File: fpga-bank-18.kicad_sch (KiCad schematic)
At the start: 1 part

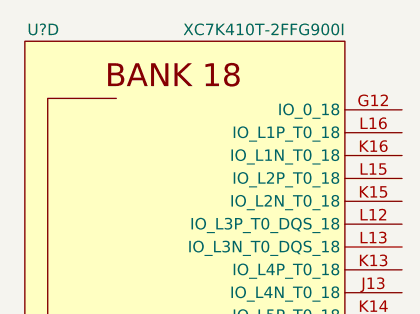
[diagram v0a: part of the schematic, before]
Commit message: Fix FPGA symbol
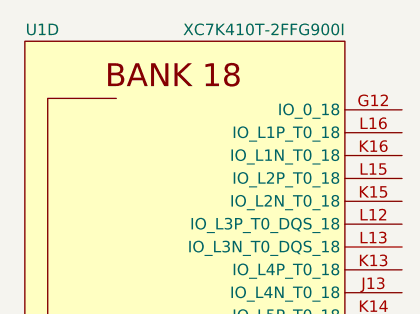
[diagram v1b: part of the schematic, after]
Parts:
- gave numbers to parts that had none: 1
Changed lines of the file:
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@@
     (rev "0.0.99")
   )
-  (symbol (lib_name "XC7K410T-2FFG900I_1") (lib_id "antmicroMicrocontrollers:XC7K410T-2FFG900I") (at 119.38 144.78 0) (unit 4)
+  (symbol (lib_id "antmicroMicrocontrollers:XC7K410T-2FFG900I") (at 119.38 144.78 0) (unit 4)
     (in_bom yes) (on_board yes)
-    (property "Reference" "U?" (id 0) (at 105.41 74.93 0)
+    (property "Reference" "U1" (id 0) (at 105.41 74.93 0)
       (effects (font (size 1.27 1.27)) (justify right))
     )

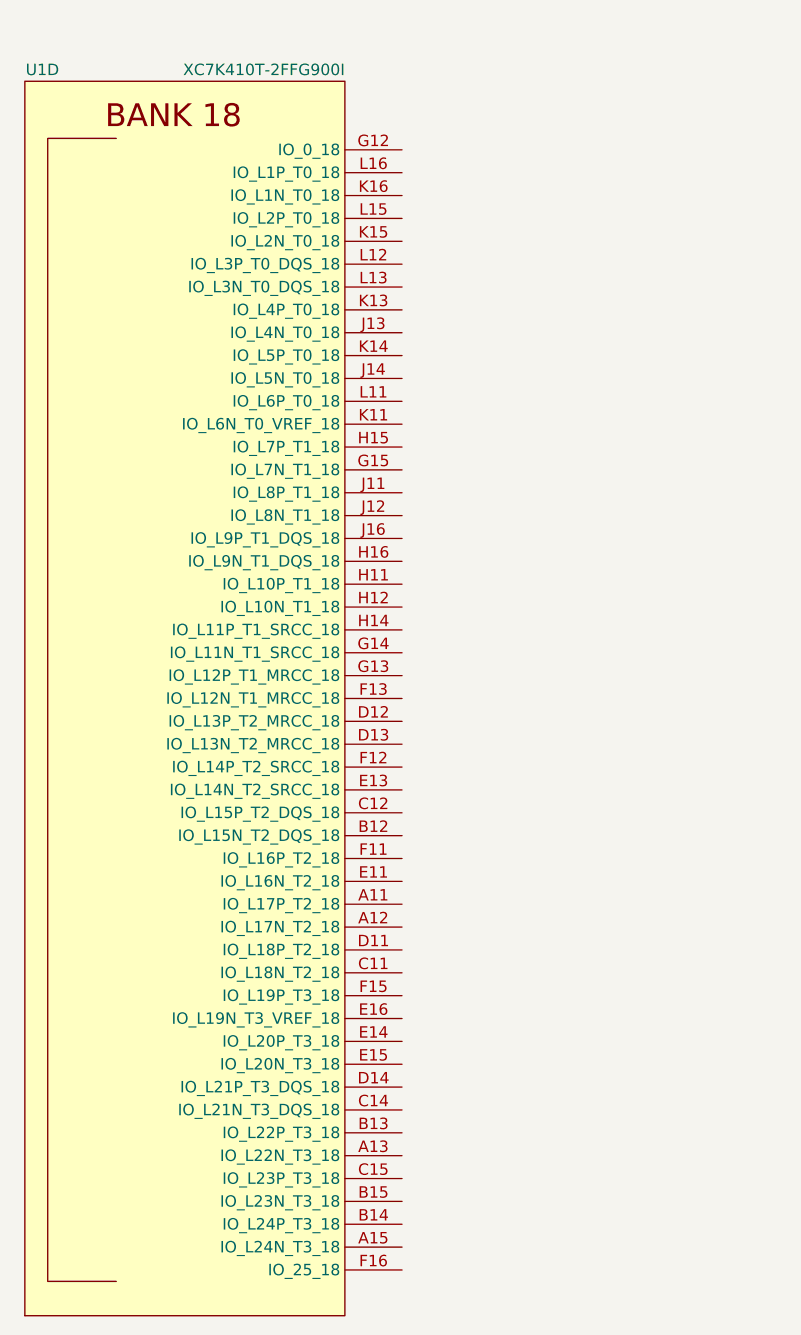
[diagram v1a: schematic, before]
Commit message: Connect IO bank 15 and MGT bank 115 and 116 to FMC+
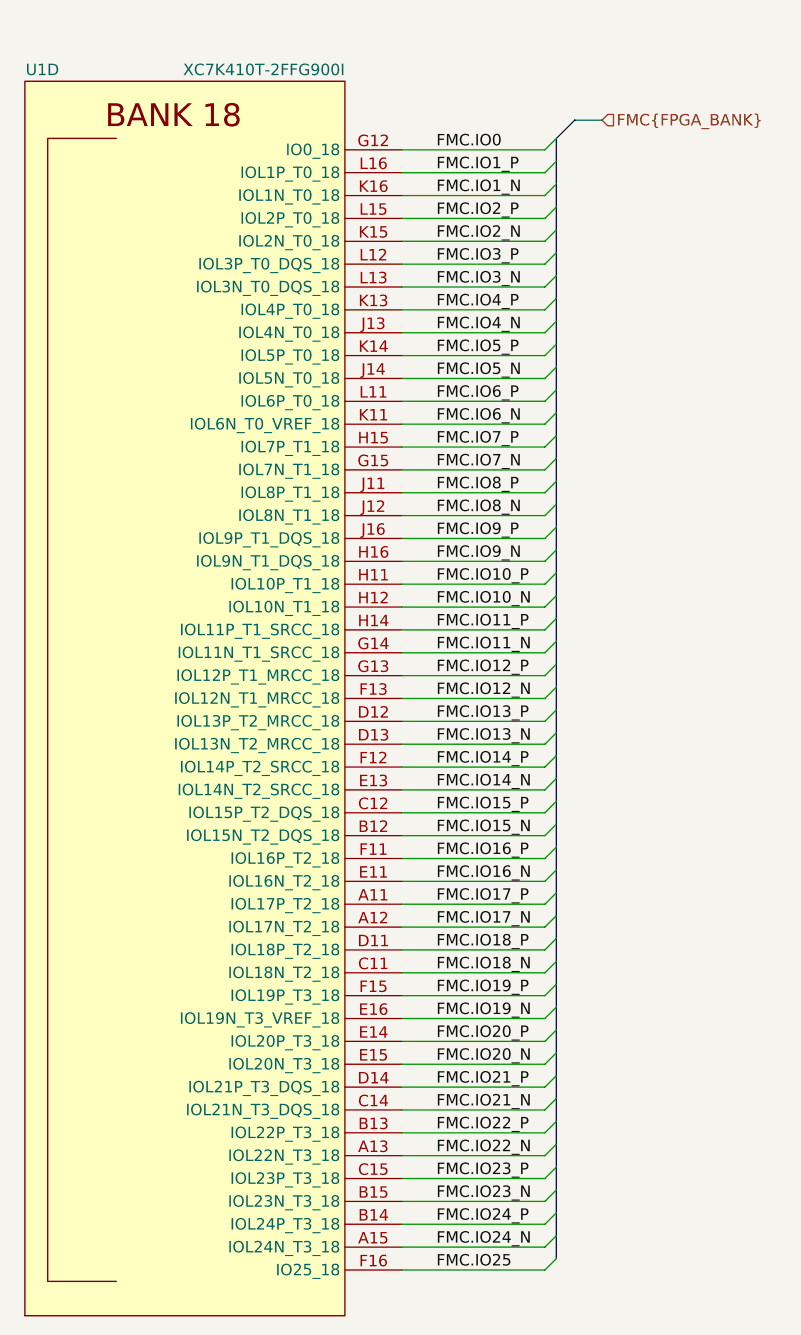
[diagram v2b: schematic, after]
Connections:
- net FMC.IO17_P: now reaches U1.A11 (IOL17P_T2_18)
- net FMC.IO17_N: now reaches U1.A12 (IOL17N_T2_18)
- net FMC.IO22_N: now reaches U1.A13 (IOL22N_T3_18)
- net FMC.IO24_N: now reaches U1.A15 (IOL24N_T3_18)
- net FMC.IO15_N: now reaches U1.B12 (IOL15N_T2_DQS_18)
- net FMC.IO22_P: now reaches U1.B13 (IOL22P_T3_18)
- net FMC.IO24_P: now reaches U1.B14 (IOL24P_T3_18)
- net FMC.IO23_N: now reaches U1.B15 (IOL23N_T3_18)
- net FMC.IO18_N: now reaches U1.C11 (IOL18N_T2_18)
- net FMC.IO15_P: now reaches U1.C12 (IOL15P_T2_DQS_18)
- net FMC.IO21_N: now reaches U1.C14 (IOL21N_T3_DQS_18)
- net FMC.IO23_P: now reaches U1.C15 (IOL23P_T3_18)
- net FMC.IO18_P: now reaches U1.D11 (IOL18P_T2_18)
- net FMC.IO13_P: now reaches U1.D12 (IOL13P_T2_MRCC_18)
- net FMC.IO13_N: now reaches U1.D13 (IOL13N_T2_MRCC_18)
- net FMC.IO21_P: now reaches U1.D14 (IOL21P_T3_DQS_18)
- net FMC.IO16_N: now reaches U1.E11 (IOL16N_T2_18)
- net FMC.IO14_N: now reaches U1.E13 (IOL14N_T2_SRCC_18)
- net FMC.IO20_P: now reaches U1.E14 (IOL20P_T3_18)
- net FMC.IO20_N: now reaches U1.E15 (IOL20N_T3_18)
- net FMC.IO19_N: now reaches U1.E16 (IOL19N_T3_VREF_18)
- net FMC.IO16_P: now reaches U1.F11 (IOL16P_T2_18)
- net FMC.IO14_P: now reaches U1.F12 (IOL14P_T2_SRCC_18)
- net FMC.IO12_N: now reaches U1.F13 (IOL12N_T1_MRCC_18)
- net FMC.IO19_P: now reaches U1.F15 (IOL19P_T3_18)
- net FMC.IO25: now reaches U1.F16 (IO25_18)
- net FMC.IO0: now reaches U1.G12 (IO0_18)
- net FMC.IO12_P: now reaches U1.G13 (IOL12P_T1_MRCC_18)
- net FMC.IO11_N: now reaches U1.G14 (IOL11N_T1_SRCC_18)
- net FMC.IO7_N: now reaches U1.G15 (IOL7N_T1_18)
- net FMC.IO10_P: now reaches U1.H11 (IOL10P_T1_18)
- net FMC.IO10_N: now reaches U1.H12 (IOL10N_T1_18)
- net FMC.IO11_P: now reaches U1.H14 (IOL11P_T1_SRCC_18)
- net FMC.IO7_P: now reaches U1.H15 (IOL7P_T1_18)
- net FMC.IO9_N: now reaches U1.H16 (IOL9N_T1_DQS_18)
- net FMC.IO8_P: now reaches U1.J11 (IOL8P_T1_18)
- net FMC.IO8_N: now reaches U1.J12 (IOL8N_T1_18)
- net FMC.IO4_N: now reaches U1.J13 (IOL4N_T0_18)
- net FMC.IO5_N: now reaches U1.J14 (IOL5N_T0_18)
- net FMC.IO9_P: now reaches U1.J16 (IOL9P_T1_DQS_18)
- net FMC.IO6_N: now reaches U1.K11 (IOL6N_T0_VREF_18)
- net FMC.IO4_P: now reaches U1.K13 (IOL4P_T0_18)
- net FMC.IO5_P: now reaches U1.K14 (IOL5P_T0_18)
- net FMC.IO2_N: now reaches U1.K15 (IOL2N_T0_18)
- net FMC.IO1_N: now reaches U1.K16 (IOL1N_T0_18)
- net FMC.IO6_P: now reaches U1.L11 (IOL6P_T0_18)
- net FMC.IO3_P: now reaches U1.L12 (IOL3P_T0_DQS_18)
- net FMC.IO3_N: now reaches U1.L13 (IOL3N_T0_DQS_18)
- net FMC.IO2_P: now reaches U1.L15 (IOL2P_T0_18)
- net FMC.IO1_P: now reaches U1.L16 (IOL1P_T0_18)

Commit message: Loclib
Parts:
- U1: footprint antmicro-footprints:xc7k410t-2ffg900I -> K410T-devboard-footprints:xc7k410t-2ffg900I; symbol antmicroMicrocontrollers:XC7K410T-2FFG900I -> K410T-devboard:XC7K410T-2FFG900I

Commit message: Bump revision to 1.0.0. Update name on schematic and PCB sheets
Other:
- title: K410T devboard -> Kintex 410T devboard

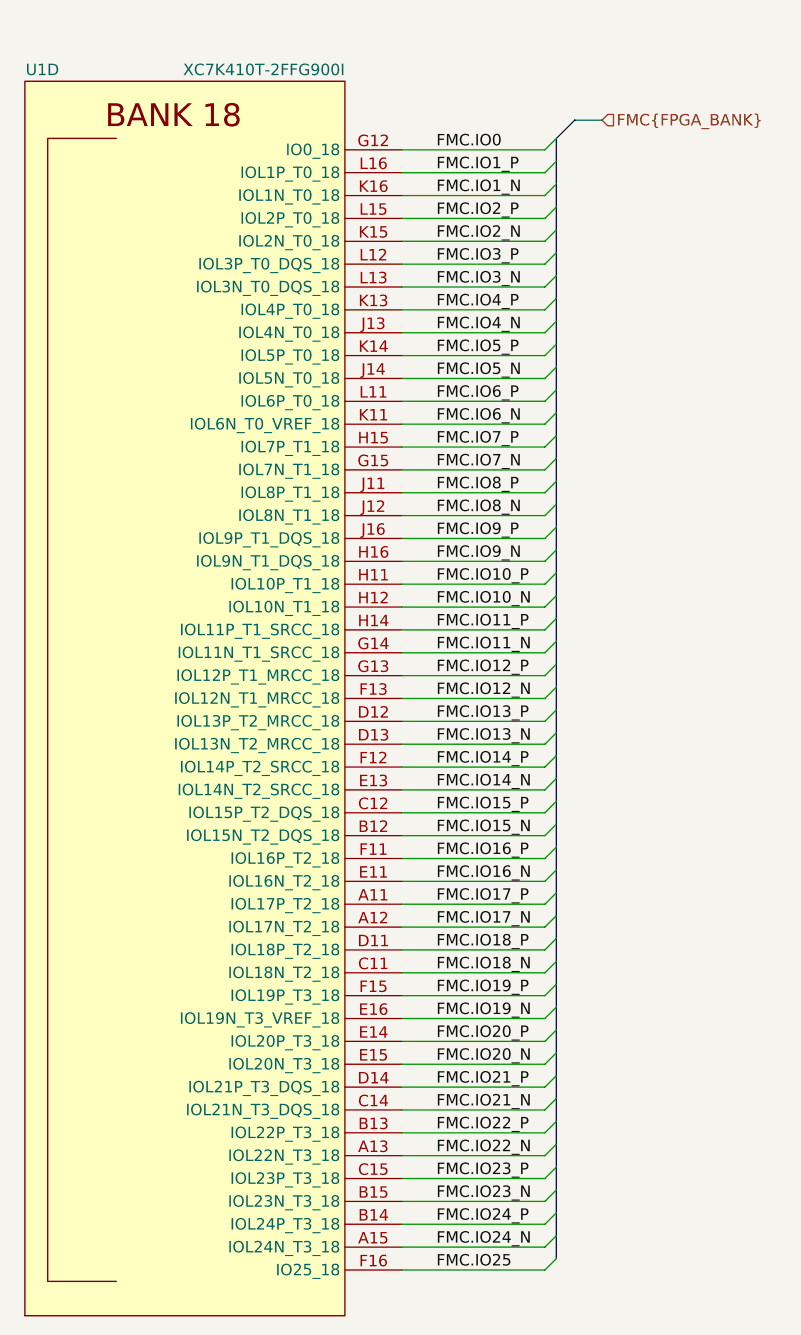
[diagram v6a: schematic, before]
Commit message: Introduce component standardization
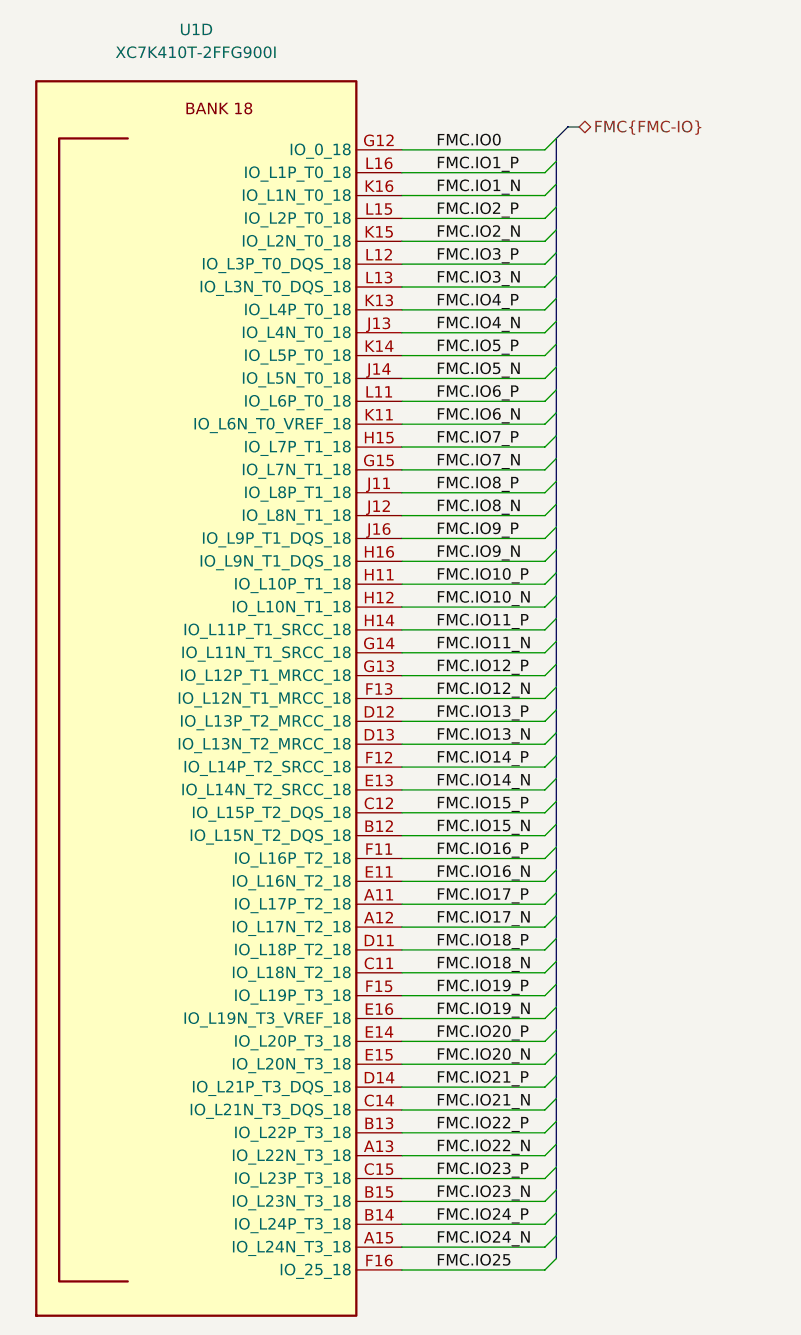
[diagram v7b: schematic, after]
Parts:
- U1: Author (none) -> Antmicro; License (none) -> Apache-2.0
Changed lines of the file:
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@@
     (title "Kintex 410T devboard")
     (date "2023-02-01")
-    (rev "1.0.0")
+    (rev "1.1.1")
   )
   (bus_entry (at 159.385 187.96) (size 1.27 -1.27)
@@
     (stroke (width 0) (type default) (color 0 0 0 0))
   )
+  (bus (pts (xy 161.925 81.28) (xy 163.195 81.28))
+    (stroke (width 0) (type default) (color 0 0 0 0))
+  )
   (wire (pts (xy 143.51 132.08) (xy 159.385 132.08))
     (stroke (width 0) (type default) (color 0 0 0 0))
@@
     (stroke (width 0) (type default) (color 0 0 0 0))
   )
+  (bus (pts (xy 160.655 82.55) (xy 161.925 81.28))
+    (stroke (width 0) (type default) (color 0 0 0 0))
+  )
   (bus (pts (xy 160.655 97.79) (xy 160.655 100.33))
     (stroke (width 0) (type default) (color 0 0 0 0))
@@
     (stroke (width 0) (type default) (color 0 0 0 0))
   )
-  (bus (pts (xy 162.687 80.518) (xy 160.655 82.55))
-    (stroke (width 0) (type default) (color 0 0 0 0))
-  )
   (bus (pts (xy 160.655 201.93) (xy 160.655 204.47))
     (stroke (width 0) (type default) (color 0 0 0 0))
@@
     (stroke (width 0) (type default) (color 0 0 0 0))
   )
-  (bus (pts (xy 162.687 80.518) (xy 165.735 80.518))
-    (stroke (width 0) (type default) (color 0 0 0 0))
-  )
   (wire (pts (xy 143.51 172.72) (xy 159.385 172.72))
     (stroke (width 0) (type default) (color 0 0 0 0))
@@
     (effects (font (size 1.27 1.27)) (justify left bottom))
   )
-  (hierarchical_label "FMC{FPGA_BANK}" (shape input) (at 165.735 80.518 0)
+  (hierarchical_label "FMC{FMC-IO}" (shape bidirectional) (at 163.195 81.28 0)
     (effects (font (size 1.27 1.27)) (justify left))
   )
-  (symbol (lib_id "K410T-devboard:XC7K410T-2FFG900I") (at 119.38 144.78 0) (unit 4)
-    (in_bom yes) (on_board yes)
-    (property "Reference" "U1" (id 0) (at 105.41 74.93 0)
-      (effects (font (size 1.27 1.27)) (justify right))
+  (symbol (lib_id "K410T-devboard:XC7K410T-2FFG900I") (at 143.51 83.82 0) (unit 4)
+    (in_bom yes) (on_board yes) (fields_autoplaced)
+    (property "Reference" "U1" (id 0) (at 120.65 70.485 0)
+      (effects (font (size 1.27 1.27) (thickness 0.15)))
+    )
+    (property "Value" "XC7K410T-2FFG900I" (id 1) (at 120.65 73.025 0)
+      (effects (font (size 1.27 1.27) (thickness 0.15)))
+    )
+    (property "Footprint" "K410T-devboard-footprints:xc7k410t-2ffg900I" (id 2) (at 143.51 57.15 0)
+      (effects (font (size 1.27 1.27) (thickness 0.15)) (justify left bottom) hide)
     )
-    (property "Value" "XC7K410T-2FFG900I" (id 1) (at 137.16 74.93 0)
-      (effects (font (size 1.27 1.27)) (justify right))
+    (property "Datasheet" "https://eu.mouser.com/datasheet/2/903/ds180_7Series_Overview-1591537.pdf" (id 3) (at 143.51 59.69 0)
+      (effects (font (size 1.27 1.27) (thickness 0.15)) (justify left bottom) hide)
     )
-    (property "Footprint" "K410T-devboard-footprints:xc7k410t-2ffg900I" (id 2) (at 119.38 219.71 0)
-      (effects (font (size 1.27 1.27)) hide)
+    (property "Manufacturer" "Xilinx" (id 4) (at 143.51 62.23 0)
+      (effects (font (size 1.27 1.27) (thickness 0.15)) (justify left bottom) hide)
     )
-    (property "Datasheet" "https://eu.mouser.com/datasheet/2/903/ds180_7Series_Overview-1591537.pdf" (id 3) (at 119.38 222.25 0)
-      (effects (font (size 1.27 1.27)) hide)
+    (property "MPN" "XC7K410T-2FFG900I" (id 5) (at 143.51 64.77 0)
+      (effects (font (size 1.27 1.27) (thickness 0.15)) (justify left bottom) hide)
     )
-    (property "Manufacturer" "Xilinx" (id 4) (at 119.38 214.63 0)
-      (effects (font (size 1.27 1.27)) hide)
+    (property "Author" "Antmicro" (id 6) (at 143.51 67.31 0)
+      (effects (font (size 1.27 1.27) (thickness 0.15)) (justify left bottom) hide)
     )
-    (property "MPN" "XC7K410T-2FFG900I" (id 5) (at 119.38 217.17 0)
-      (effects (font (size 1.27 1.27)) hide)
+    (property "License" "Apache-2.0" (id 7) (at 143.51 69.85 0)
+      (effects (font (size 1.27 1.27) (thickness 0.15)) (justify left bottom) hide)
     )
     (pin "AA20")
@@
     (pin "Y12")
     (pin "Y22")
-    (pin "C10")
-    (pin "M11")
-    (pin "M13")
-    (pin "M15")
-    (pin "M17")
-    (pin "N10")
-    (pin "N12")
-    (pin "N14")
-    (pin "N16")
-    (pin "N18")
-    (pin "P11")
-    (pin "P13")
-    (pin "P14")
-    (pin "P15")
-    (pin "P17")
-    (pin "R10")
-    (pin "R12")
-    (pin "R16")
-    (pin "R18")
-    (pin "T11")
-    (pin "T13")
-    (pin "T17")
-    (pin "U10")
-    (pin "U12")
-    (pin "U16")
-    (pin "U18")
-    (pin "V11")
-    (pin "V13")
-    (pin "V15")
-    (pin "V17")
-    (pin "W10")
-    (pin "W12")
-    (pin "W14")
-    (pin "W16")
-    (pin "W18")
     (pin "A1")
     (pin "A14")
@@
     (pin "B9")
     (pin "C1")
+    (pin "C10")
     (pin "C18")
     (pin "C2")
@@
     (pin "L6")
     (pin "L9")
+    (pin "M11")
     (pin "M12")
+    (pin "M13")
     (pin "M14")
+    (pin "M15")
     (pin "M16")
+    (pin "M17")
     (pin "M18")
     (pin "M21")
@@
     (pin "M9")
     (pin "N1")
+    (pin "N10")
     (pin "N11")
+    (pin "N12")
     (pin "N13")
+    (pin "N14")
     (pin "N15")
+    (pin "N16")
     (pin "N17")
+    (pin "N18")
     (pin "N2")
     (pin "N28")
@@
     (pin "N9")
     (pin "P10")
+    (pin "P11")
     (pin "P12")
+    (pin "P13")
+    (pin "P14")
+    (pin "P15")
     (pin "P16")
+    (pin "P17")
     (pin "P18")
     (pin "P25")
@@
     (pin "P9")
     (pin "R1")
+    (pin "R10")
     (pin "R11")
+    (pin "R12")
     (pin "R13")
+    (pin "R16")
     (pin "R17")
+    (pin "R18")
     (pin "R2")
     (pin "R22")
@@
     (pin "R9")
     (pin "T10")
+    (pin "T11")
     (pin "T12")
+    (pin "T13")
     (pin "T16")
+    (pin "T17")
     (pin "T18")
     (pin "T19")
@@
     (pin "T8")
     (pin "U1")
+    (pin "U10")
     (pin "U11")
+    (pin "U12")
     (pin "U13")
+    (pin "U16")
     (pin "U17")
+    (pin "U18")
     (pin "U2")
     (pin "U26")
@@
     (pin "U9")
     (pin "V10")
+    (pin "V11")
     (pin "V12")
+    (pin "V13")
     (pin "V14")
+    (pin "V15")
     (pin "V16")
+    (pin "V17")
     (pin "V18")
     (pin "V23")
@@
     (pin "V9")
     (pin "W1")
+    (pin "W10")
     (pin "W11")
+    (pin "W12")
     (pin "W13")
+    (pin "W14")
     (pin "W15")
+    (pin "W16")
     (pin "W17")
+    (pin "W18")
     (pin "W2")
     (pin "W20")
